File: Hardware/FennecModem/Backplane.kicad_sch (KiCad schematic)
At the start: 28 parts, among them J1 SEL_ADDR, J3 EN_ADDR, Q2 AO3401A, Q801 MMBT3904, U2 L7805, U3 SN74LVC1T45DBV, U4 SN74LVC1T45DBV, U5 SN74LVC1T45DBV, U6 SN74LVC1T45DBV, U7 SN74LVC1T45DBV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

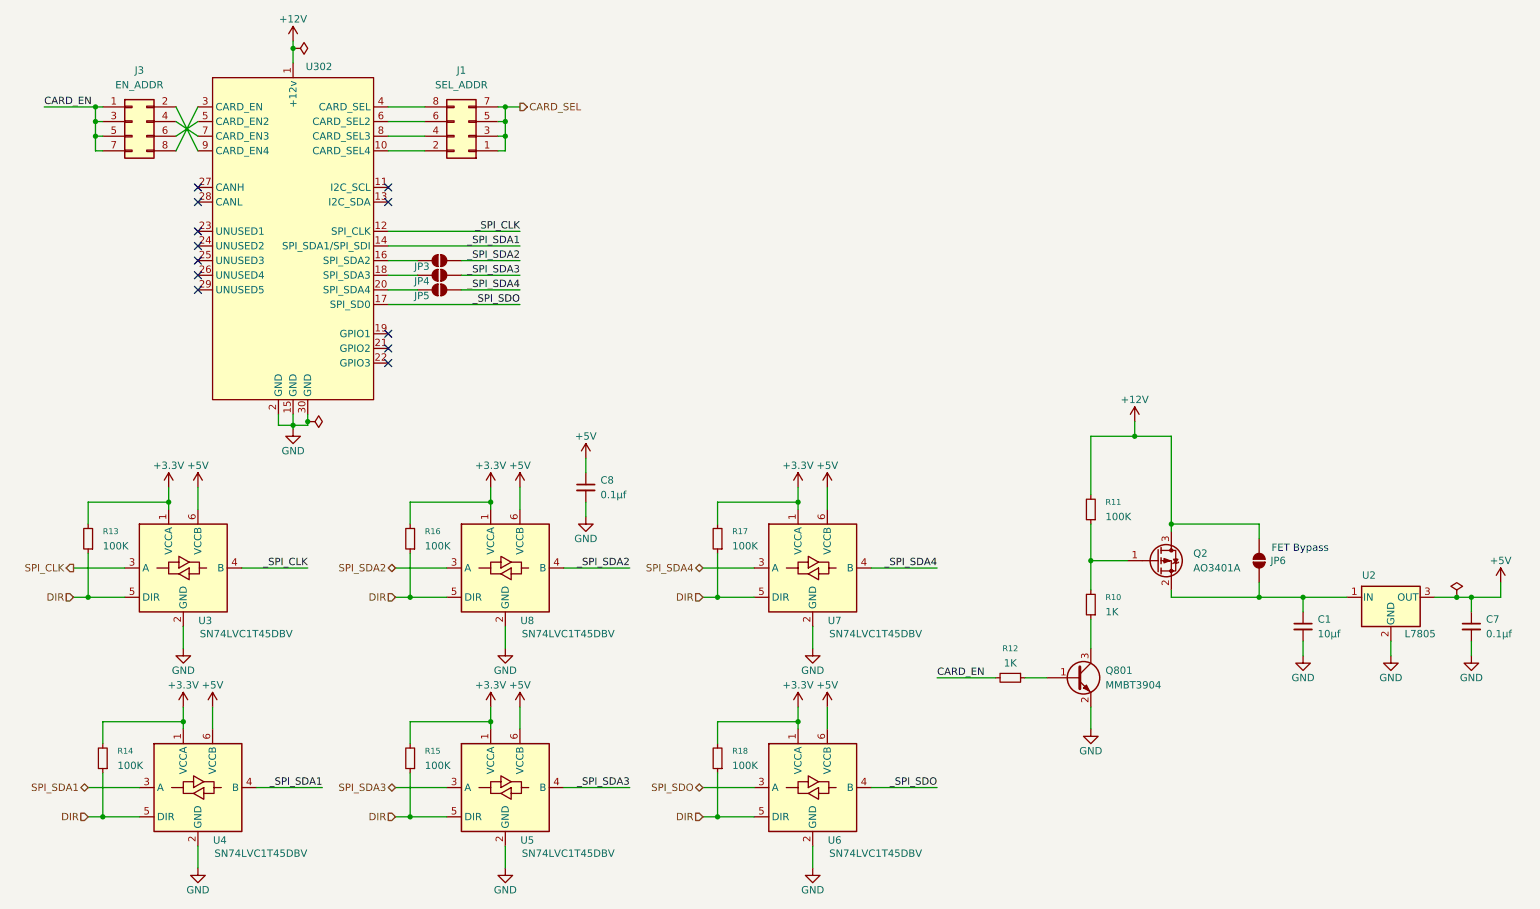
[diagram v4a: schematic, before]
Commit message: Implement new power supply
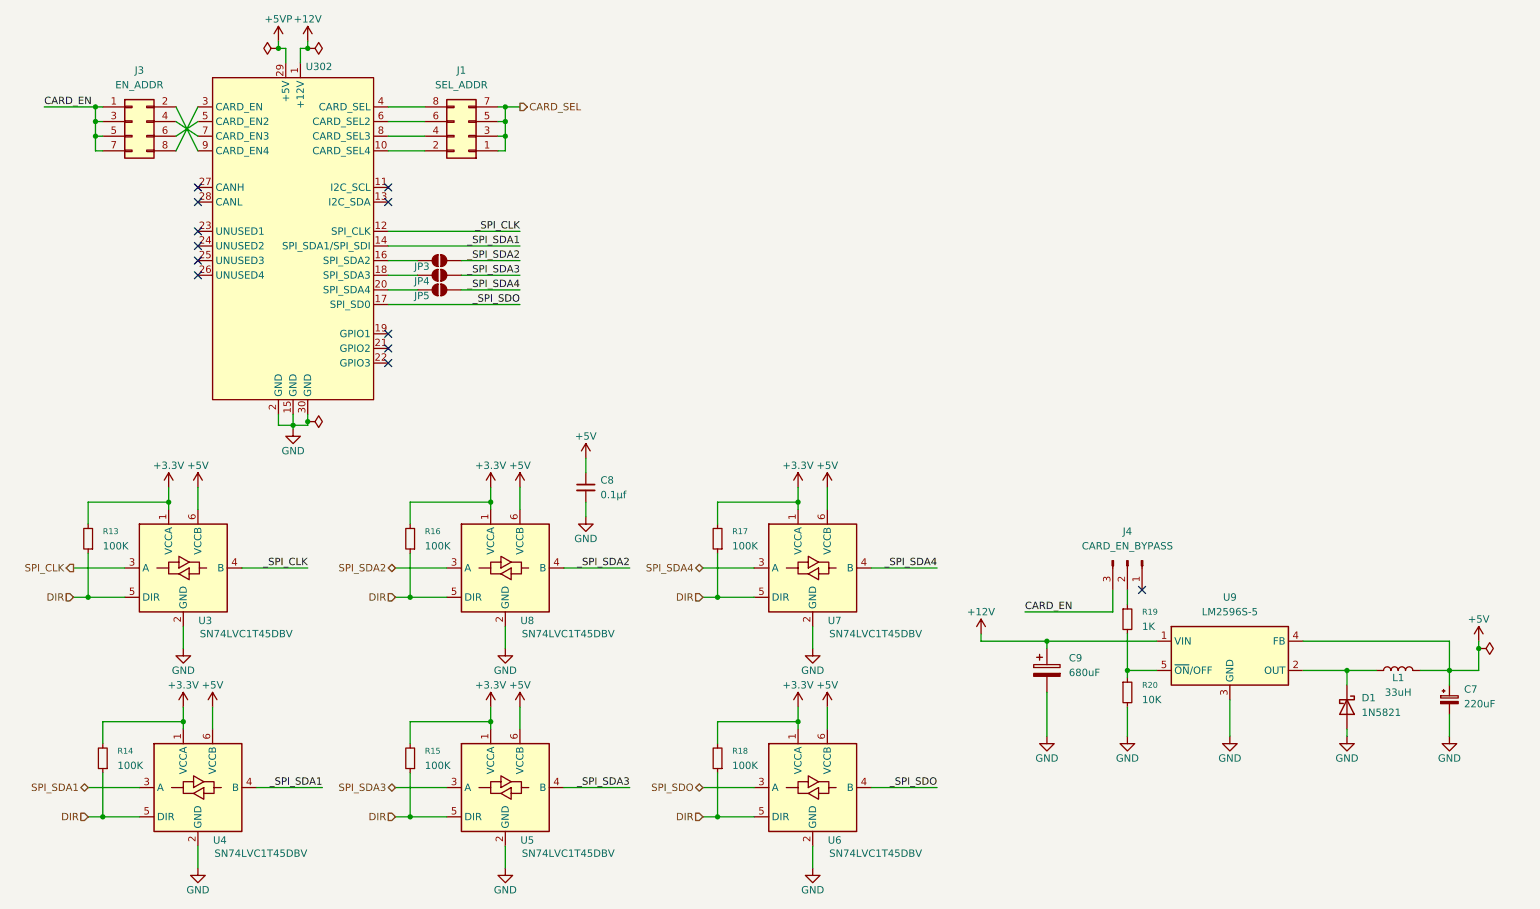
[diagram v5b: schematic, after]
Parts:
- removed C1: 10μf, Capacitor_SMD:C_0805_2012Metric, symbol Device:C_Small
- removed C7: 0.1μf, Capacitor_SMD:C_0805_2012Metric, symbol Device:C_Small
- removed JP6: SolderJumper_2_Open, Jumper:SolderJumper-2_P1.3mm_Open_TrianglePad1.0x1.5mm, symbol Jumper:SolderJumper_2_Open
- removed Q2: AO3401A, Package_TO_SOT_SMD:SOT-23, symbol Transistor_FET:AO3401A
- removed Q801: MMBT3904, Package_TO_SOT_SMD:SOT-23, symbol Transistor_BJT:MMBT3904
- removed R10, R12: 1K, Resistor_SMD:R_0805_2012Metric, symbol Device:R_Small
- removed R11: 100K, Resistor_SMD:R_0805_2012Metric, symbol Device:R_Small
- removed U2: L7805, Package_TO_SOT_THT:TO-220-3_Horizontal_TabDown, symbol Regulator_Linear:L7805
- added C7: 220uF, Capacitor_THT:CP_Radial_D5.0mm_P2.50mm, symbol Device:C_Polarized_Small
- added C9: 680uF, Capacitor_THT:CP_Radial_D10.0mm_P5.00mm, symbol Device:C_Polarized
- added D1: 1N5821, Diode_THT:D_DO-41_SOD81_P5.08mm_Vertical_AnodeUp, symbol Diode:1N5821
- added J4: CARD_EN_BYPASS, Connector_PinHeader_2.54mm:PinHeader_1x03_P2.54mm_Vertical, symbol Connector:Conn_01x03_Pin
- added L1: 33uH, Inductor_SMD:L_6.3x6.3_H3, symbol Device:L
- added R19: 1K, Resistor_SMD:R_0805_2012Metric, symbol Device:R_Small
- added R20: 10K, Resistor_SMD:R_0805_2012Metric, symbol Device:R_Small
- added U9: LM2596S-5, Package_TO_SOT_SMD:TO-263-5_TabPin3, symbol Regulator_Switching:LM2596S-5
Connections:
- net +12V: now also C9.1, U9.1 (VIN)
- net +5V: now also C7.1, L1.2, U9.4 (FB)
- net CARD_EN: now also J4.3 (Pin_3)
- net GND: now also C7.2, C9.2, D1.2 (A), R20.2, U9.3 (GND)
- net +5VP: now reaches U302.29 (+5V)
- new net: D1.1 (K), L1.1, U9.2 (OUT)
- new net: R19.2, R20.1, U9.5 (~{ON}/OFF)
- new net: J4.2 (Pin_2), R19.1
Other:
- note removed: "FET Bypass"

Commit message: Add new driver system
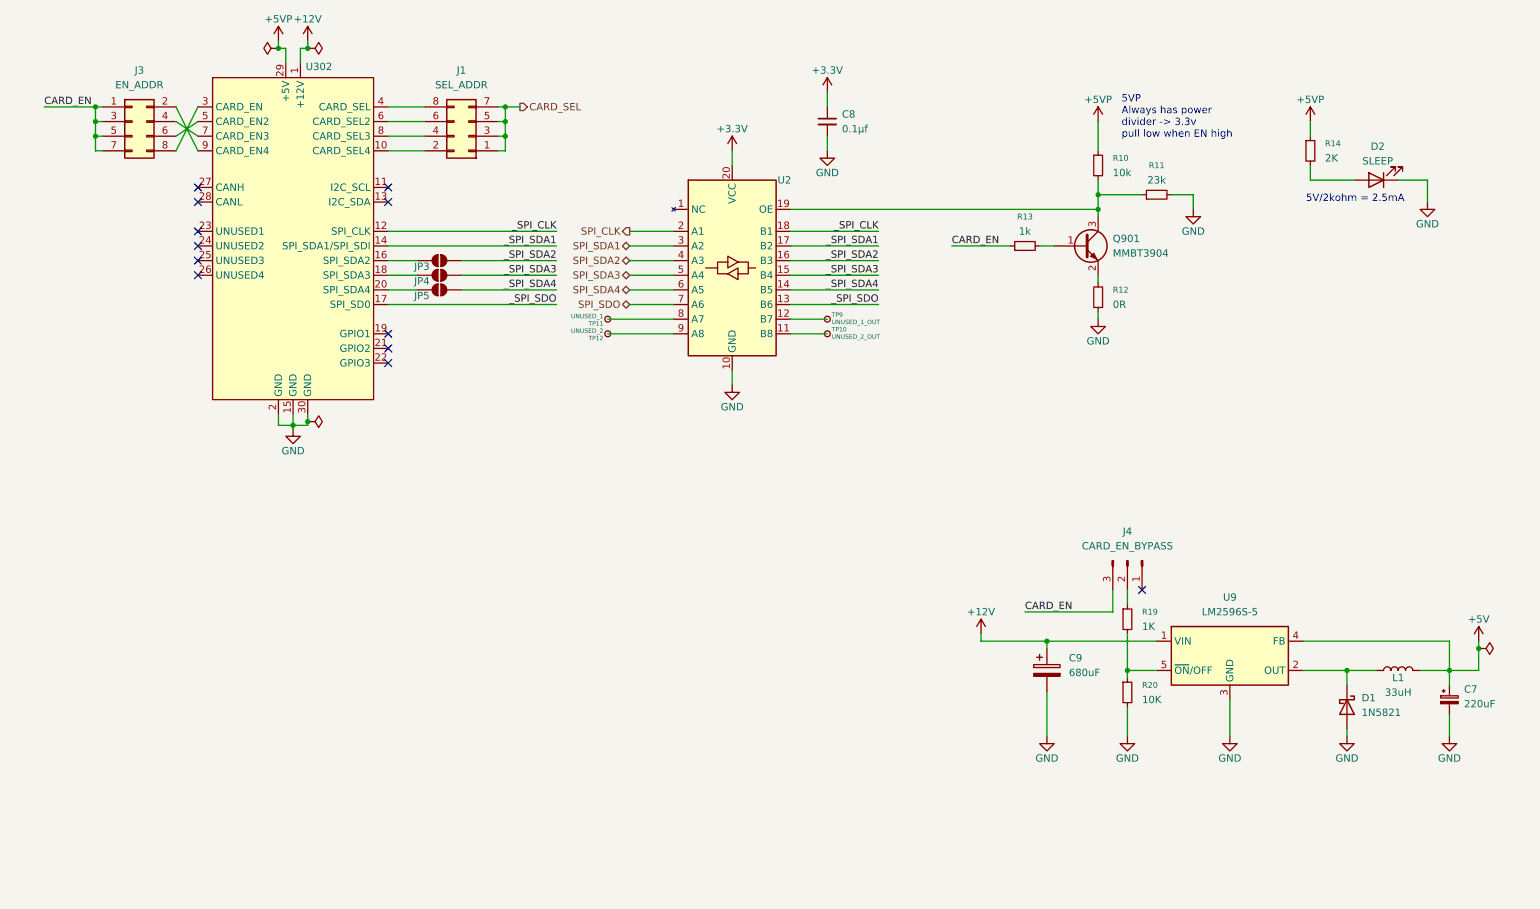
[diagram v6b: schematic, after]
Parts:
- removed R15, R16, R17, R18: 100K, Resistor_SMD:R_0805_2012Metric, symbol Device:R_Small
- removed U3, U4, U5, U6, U7, U8: SN74LVC1T45DBV, Package_TO_SOT_SMD:SOT-23-6, symbol Logic_LevelTranslator:SN74LVC1T45DBV
- added D2: SLEEP, LED_THT:LED_D3.0mm, symbol Device:LED
- added Q901: MMBT3904, Package_TO_SOT_SMD:SOT-23, symbol Transistor_BJT:MMBT3904
- added R10: 10k, Resistor_SMD:R_0805_2012Metric, symbol Device:R_Small
- added R11: 23k, Resistor_SMD:R_0805_2012Metric, symbol Device:R_Small
- added R12: 0R, Resistor_SMD:R_0805_2012Metric, symbol Device:R_Small
- added TP10: UNUSED_2_OUT, TestPoint:TestPoint_Bridge_Pitch2.0mm_Drill0.7mm, symbol Connector:TestPoint_Small
- added TP11: UNUSED_1, TestPoint:TestPoint_Bridge_Pitch2.0mm_Drill0.7mm, symbol Connector:TestPoint_Small
- added TP12: UNUSED_2, TestPoint:TestPoint_Bridge_Pitch2.0mm_Drill0.7mm, symbol Connector:TestPoint_Small
- added TP9: UNUSED_1_OUT, TestPoint:TestPoint_Bridge_Pitch2.0mm_Drill0.7mm, symbol Connector:TestPoint_Small
- added U2: SN74CBTLV3245A, Package_SO:SSOP-20_3.9x8.7mm_P0.635mm, symbol KenwoodFox:SN74CBTLV3245
- R13: value 100K -> 1k
- R14: value 100K -> 2K
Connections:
- net +3.3V: now also C8.1, U2.20 (VCC); no longer R13.2, R14.2
- net +5V: no longer C8.1
- net +5VP: now also R14.1, R10.1
- net CARD_EN: now also R13.1
- net GND: now also D2.1 (K), R11.2, R12.1, U2.10 (GND)
- net SPI_CLK: now also U2.2 (A1)
- net SPI_SDA1: now also U2.3 (A2)
- net SPI_SDA2: now also U2.4 (A3)
- net SPI_SDA3: now also U2.5 (A4)
- net SPI_SDA4: now also U2.6 (A5)
- net SPI_SDO: now also U2.7 (A6)
- net _SPI_CLK: now also U2.18 (B1)
- net _SPI_SDA1: now also U2.17 (B2)
- net _SPI_SDA2: now also U2.16 (B3)
- net _SPI_SDA3: now also U2.15 (B4)
- net _SPI_SDA4: now also U2.14 (B5)
- net _SPI_SDO: now also U2.13 (B6)
- removed net DIR: R13.1, R14.1
- new net: D2.2 (A), R14.2
- new net: TP9.1, U2.12 (B7)
- new net: TP11.1, U2.8 (A7)
- new net: Q901.2 (E), R12.2
- new net: Q901.3 (C), R10.2, R11.1, U2.19 (OE)
- new net: TP10.1, U2.11 (B8)
- new net: TP12.1, U2.9 (A8)
- new net: Q901.1 (B), R13.2
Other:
- note added: "5V/2kohm = 2.5mA"
- note added: "5VP Always has power divider -> 3.3v pull low when EN high"
- moved on the sheet: C8

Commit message: Impl last of overall
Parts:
- added JP1: SolderJumper_2_Open, Jumper:SolderJumper-2_P1.3mm_Open_TrianglePad1.0x1.5mm, symbol Jumper:SolderJumper_2_Open
- D2: footprint LED_THT:LED_D3.0mm -> LED_SMD:LED_0805_2012Metric
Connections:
- net at Q901.3 (C), R10.2, R11.1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: now also JP1.1 (A)
- net at Q901.1 (B), R13.2: now also JP1.2 (B)
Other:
- moved on the sheet: Q901, R12, R13
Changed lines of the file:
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@@
 	)
 	(junction
+		(at 194.31 64.77)
+		(diameter 0)
+		(color 0 0 0 0)
+	)
+	(junction
 		(at 270.51 140.97)
 		(diameter 0)
@@
 	)
 	(junction
+		(at 194.31 72.39)
+		(diameter 0)
+		(color 0 0 0 0)
+	)
+	(junction
 		(at 30.48 52.07)
 		(diameter 0)
@@
 	(wire
 		(pts
-			(xy 179.07 71.12) (xy 189.23 71.12)
+			(xy 171.45 72.39) (xy 181.61 72.39)
+		)
+		(stroke
+			(width 0)
+			(type default)
+		)
+	)
+	(wire
+		(pts
+			(xy 194.31 72.39) (xy 196.85 72.39)
 		)
 		(stroke
@@
 	(wire
 		(pts
-			(xy 204.47 64.77) (xy 204.47 66.04)
+			(xy 204.47 64.77) (xy 204.47 67.31)
 		)
 		(stroke
@@
 	(wire
 		(pts
-			(xy 204.47 76.2) (xy 204.47 77.47)
+			(xy 204.47 77.47) (xy 204.47 78.74)
 		)
 		(stroke
@@
 	(wire
 		(pts
-			(xy 151.13 64.77) (xy 204.47 64.77)
+			(xy 151.13 64.77) (xy 194.31 64.77)
 		)
 		(stroke
@@
 	(wire
 		(pts
-			(xy 204.47 82.55) (xy 204.47 83.82)
+			(xy 204.47 83.82) (xy 204.47 85.09)
 		)
 		(stroke
@@
 	(wire
 		(pts
+			(xy 194.31 64.77) (xy 204.47 64.77)
+		)
+		(stroke
+			(width 0)
+			(type default)
+		)
+	)
+	(wire
+		(pts
 			(xy 62.23 36.8299) (xy 62.23 36.83)
 		)
@@
 	(wire
 		(pts
-			(xy 194.31 71.12) (xy 196.85 71.12)
+			(xy 186.69 72.39) (xy 194.31 72.39)
 		)
 		(stroke
@@
 	)
 	(label "CARD_EN"
-		(at 179.07 71.12 0)
+		(at 171.45 72.39 0)
 		(effects
 			(font
@@
 	)
 	(symbol
+		(lib_id "Jumper:SolderJumper_2_Open")
+		(at 194.31 68.58 270)
+		(unit 1)
+		(exclude_from_sim no)
+		(in_bom no)
+		(on_board yes)
+		(dnp no)
+		(property "Reference" "JP1"
+			(at 197.358 68.834 90)
+			(effects
+				(font
+					(size 1.27 1.27)
+				)
+			)
+		)
+		(property "Value" "SolderJumper_2_Open"
+			(at 198.12 68.58 0)
+			(effects
+				(font
+					(size 1.27 1.27)
+				)
+				(hide yes)
+			)
+		)
+		(property "Footprint" "Jumper:SolderJumper-2_P1.3mm_Open_TrianglePad1.0x1.5mm"
+			(at 194.31 68.58 0)
+			(effects
+				(font
+					(size 1.27 1.27)
+				)
+				(hide yes)
+			)
+		)
+		(property "Datasheet" "~"
+			(at 194.31 68.58 0)
+			(effects
+				(font
+					(size 1.27 1.27)
+				)
+				(hide yes)
+			)
+		)
+		(property "Description" "Solder Jumper, 2-pole, open"
+			(at 194.31 68.58 0)
+			(effects
+				(font
+					(size 1.27 1.27)
+				)
+				(hide yes)
+			)
+		)
+		(pin "2"
+		)
+		(pin "1"
+		)
+		(instances
+			(project "FennecModem"
+				(path "/8cb1f8f8-0f28-4c6f-8a0b-e6b064917aa9/192ed9e7-ecb8-4622-a83a-67936d551760"
+					(reference "JP1")
+					(unit 1)
+				)
+			)
+		)
+	)
+	(symbol
 		(lib_id "Connector:Conn_01x03_Pin")
 		(at 209.55 125.73 270)
@@
 	(symbol
 		(lib_id "power:GND")
-		(at 204.47 83.82 0)
+		(at 204.47 85.09 0)
 		(unit 1)
 		(exclude_from_sim no)
@@
 		(dnp no)
 		(property "Reference" "#PWR026"
-			(at 204.47 90.17 0)
+			(at 204.47 91.44 0)
 			(effects
 				(font
@@
 		)
 		(property "Value" "GND"
-			(at 204.47 87.63 0)
+			(at 204.47 88.9 0)
 			(effects
 				(font
@@
 		)
 		(property "Footprint" ""
-			(at 204.47 83.82 0)
+			(at 204.47 85.09 0)
 			(effects
 				(font
@@
 		)
 		(property "Datasheet" ""
-			(at 204.47 83.82 0)
+			(at 204.47 85.09 0)
 			(effects
 				(font
@@
 		)
 		(property "Description" ""
-			(at 204.47 83.82 0)
+			(at 204.47 85.09 0)
 			(effects
 				(font
@@
 	)
 	(symbol
+		(lib_id "Device:LED")
+		(at 252.73 59.69 180)
+		(unit 1)
+		(exclude_from_sim no)
+		(in_bom yes)
+		(on_board yes)
+		(dnp no)
+		(property "Reference" "D2"
+			(at 254.635 56.515 90)
+			(effects
+				(font
+					(size 1.27 1.27)
+				)
+				(justify right)
+			)
+		)
+		(property "Value" "SLEEP"
+			(at 252.73 56.515 90)
+			(effects
+				(font
+					(size 1.27 1.27)
+				)
+				(justify right)
+			)
+		)
+		(property "Footprint" "LED_SMD:LED_0805_2012Metric"
+			(at 252.73 59.69 0)
+			(effects
+				(font
+					(size 1.27 1.27)
+				)
+				(hide yes)
+			)
+		)
+		(property "Datasheet" "~"
+			(at 252.73 59.69 0)
+			(effects
+				(font
+					(size 1.27 1.27)
+				)
+				(hide yes)
+			)
+		)
+		(property "Description" ""
+			(at 252.73 59.69 0)
+			(effects
+				(font
+					(size 1.27 1.27)
+				)
+				(hide yes)
+			)
+		)
+		(pin "1"
+		)
+		(pin "2"
+		)
+		(instances
+			(project "FennecModem"
+				(path "/8cb1f8f8-0f28-4c6f-8a0b-e6b064917aa9/192ed9e7-ecb8-4622-a83a-67936d551760"
+					(reference "D2")
+					(unit 1)
+				)
+			)
+		)
+	)
+	(symbol
 		(lib_id "power:GND")
 		(at 140.97 95.25 0)
@@
 	(symbol
 		(lib_id "Device:R_Small")
-		(at 204.47 80.01 180)
+		(at 204.47 81.28 180)
 		(unit 1)
 		(exclude_from_sim no)
@@
 		(fields_autoplaced yes)
 		(property "Reference" "R12"
-			(at 207.01 78.7399 0)
+			(at 207.01 80.0099 0)
 			(effects
 				(font
@@
 		)
 		(property "Value" "0R"
-			(at 207.01 81.2799 0)
+			(at 207.01 82.5499 0)
 			(effects
 				(font
@@
 		)
 		(property "Footprint" "Resistor_SMD:R_0805_2012Metric"
-			(at 204.47 80.01 0)
+			(at 204.47 81.28 0)
 			(effects
 				(font
@@
 		)
 		(property "Datasheet" "~"
-			(at 204.47 80.01 0)
+			(at 204.47 81.28 0)
 			(effects
 				(font
@@
 		)
 		(property "Description" "Resistor, small symbol"
-			(at 204.47 80.01 0)
+			(at 204.47 81.28 0)
 			(effects
 				(font
@@
 	)
 	(symbol
-		(lib_id "Device:LED")
-		(at 252.73 59.69 180)
-		(unit 1)
-		(exclude_from_sim no)
-		(in_bom yes)
-		(on_board yes)
-		(dnp no)
-		(property "Reference" "D2"
-			(at 252.984 53.848 0)
-			(effects
-				(font
-					(size 1.27 1.27)
-				)
-			)
-		)
-		(property "Value" "SLEEP"
-			(at 252.984 56.388 0)
-			(effects
-				(font
-					(size 1.27 1.27)
-				)
-			)
-		)
-		(property "Footprint" "LED_THT:LED_D3.0mm"
-			(at 252.73 59.69 0)
-			(effects
-				(font
-					(size 1.27 1.27)
-				)
-				(hide yes)
-			)
-		)
-		(property "Datasheet" "~"
-			(at 252.73 59.69 0)
-			(effects
-				(font
-					(size 1.27 1.27)
-				)
-				(hide yes)
-			)
-		)
-		(property "Description" "Light emitting diode"
-			(at 252.73 59.69 0)
-			(effects
-				(font
-					(size 1.27 1.27)
-				)
-				(hide yes)
-			)
-		)
-		(property "Sim.Pins" "1=K 2=A"
-			(at 252.73 59.69 0)
-			(effects
-				(font
-					(size 1.27 1.27)
-				)
-				(hide yes)
-			)
-		)
-		(pin "1"
-		)
-		(pin "2"
-		)
-		(instances
-			(project ""
-				(path "/8cb1f8f8-0f28-4c6f-8a0b-e6b064917aa9/192ed9e7-ecb8-4622-a83a-67936d551760"
-					(reference "D2")
-					(unit 1)
-				)
-			)
-		)
-	)
-	(symbol
 		(lib_id "power:PWR_FLAG")
 		(at 62.23 36.8299 90)
@@
 	(symbol
 		(lib_id "Device:R_Small")
-		(at 191.77 71.12 90)
+		(at 184.15 72.39 90)
 		(unit 1)
 		(exclude_from_sim no)
@@
 		(fields_autoplaced yes)
 		(property "Reference" "R13"
-			(at 191.77 66.04 90)
+			(at 184.15 67.31 90)
 			(effects
 				(font
@@
 		)
 		(property "Value" "1k"
-			(at 191.77 68.58 90)
+			(at 184.15 69.85 90)
 			(effects
 				(font
@@
 		)
 		(property "Footprint" "Resistor_SMD:R_0805_2012Metric"
-			(at 191.77 71.12 0)
+			(at 184.15 72.39 0)
 			(effects
 				(font
@@
 		)
 		(property "Datasheet" "~"
-			(at 191.77 71.12 0)
+			(at 184.15 72.39 0)
 			(effects
 				(font
@@
 		)
 		(property "Description" "Resistor, small symbol"
-			(at 191.77 71.12 0)
+			(at 184.15 72.39 0)
 			(effects
 				(font
@@
 	(symbol
 		(lib_id "Transistor_BJT:MMBT3904")
-		(at 201.93 71.12 0)
+		(at 201.93 72.39 0)
 		(unit 1)
 		(exclude_from_sim no)
@@
 		(fields_autoplaced yes)
 		(property "Reference" "Q901"
-			(at 207.01 69.8499 0)
+			(at 207.01 71.1199 0)
 			(effects
 				(font
@@
 		)
 		(property "Value" "MMBT3904"
-			(at 207.01 72.3899 0)
+			(at 207.01 73.6599 0)
 			(effects
 				(font
@@
 		)
 		(property "Footprint" "Package_TO_SOT_SMD:SOT-23"
-			(at 207.01 73.025 0)
+			(at 207.01 74.295 0)
 			(effects
 				(font
@@
 		)
 		(property "Datasheet" "https://www.onsemi.com/pub/Collateral/2N3903-D.PDF"
-			(at 201.93 71.12 0)
+			(at 201.93 72.39 0)
 			(effects
 				(font
@@
 		)
 		(property "Description" ""
-			(at 201.93 71.12 0)
+			(at 201.93 72.39 0)
 			(effects
 				(font
